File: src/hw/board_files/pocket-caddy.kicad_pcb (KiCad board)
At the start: 4 copper layers, 68 x 100 mm, 90 parts, among them J1 USB_C_Receptacle_USB2.0_14P, J2 Screw_Terminal_01x03, J3 Conn_01x03_Pin, J4 Test_Points, J5 Conn_01x04, J6 Molex 104031-0811, Q1 PMOS, SW1 SW_PWR, SW2 RESET, SW3 BTN_2, SW4 BTN_3, SW5 BTN_1_BOOT, U1 MCP73871, U2 TPS63031DSKR, U3 ESP32-C3-WROOM-02, U4 NEO-M9N, U5 SHT30-DIS, U6 BQ27411DRZT-G1A, Y1 32.768kHz

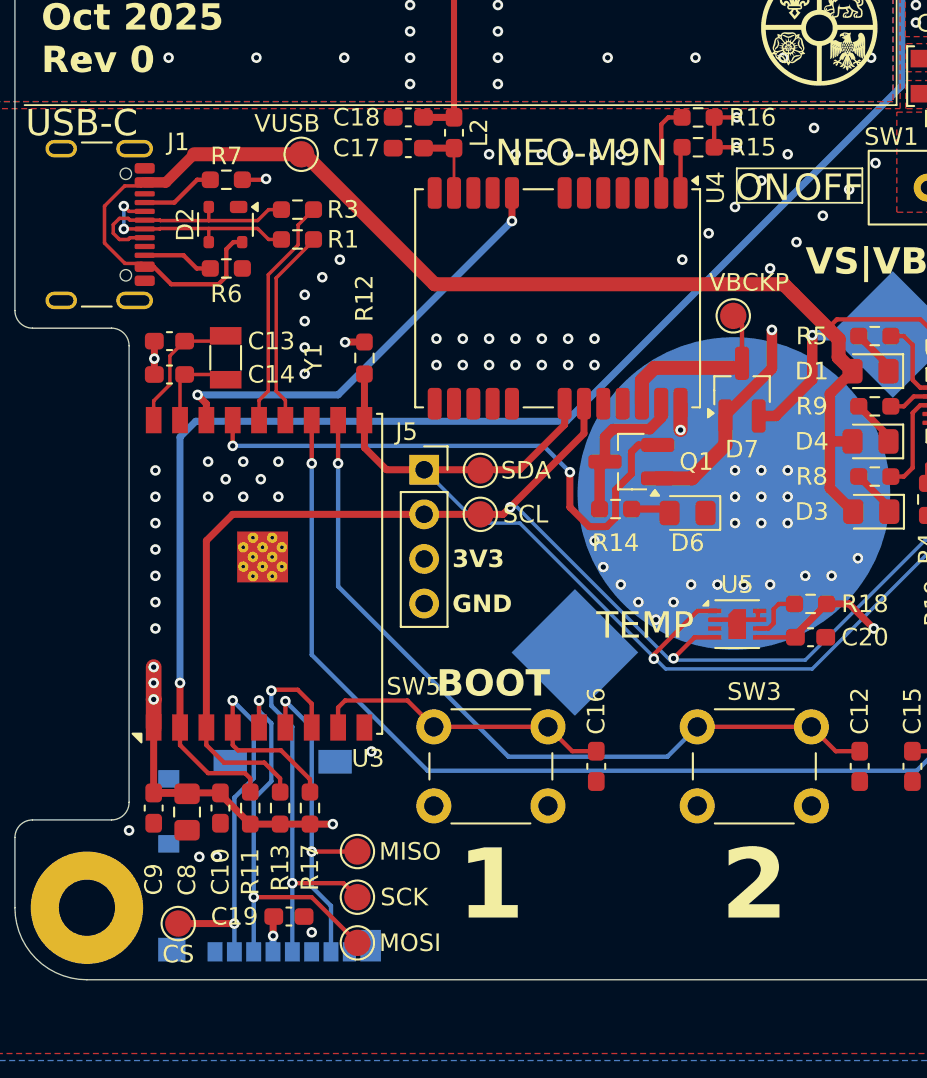
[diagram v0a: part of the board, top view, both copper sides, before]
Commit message: Initial commit, fixed esp enable RC delay circuit
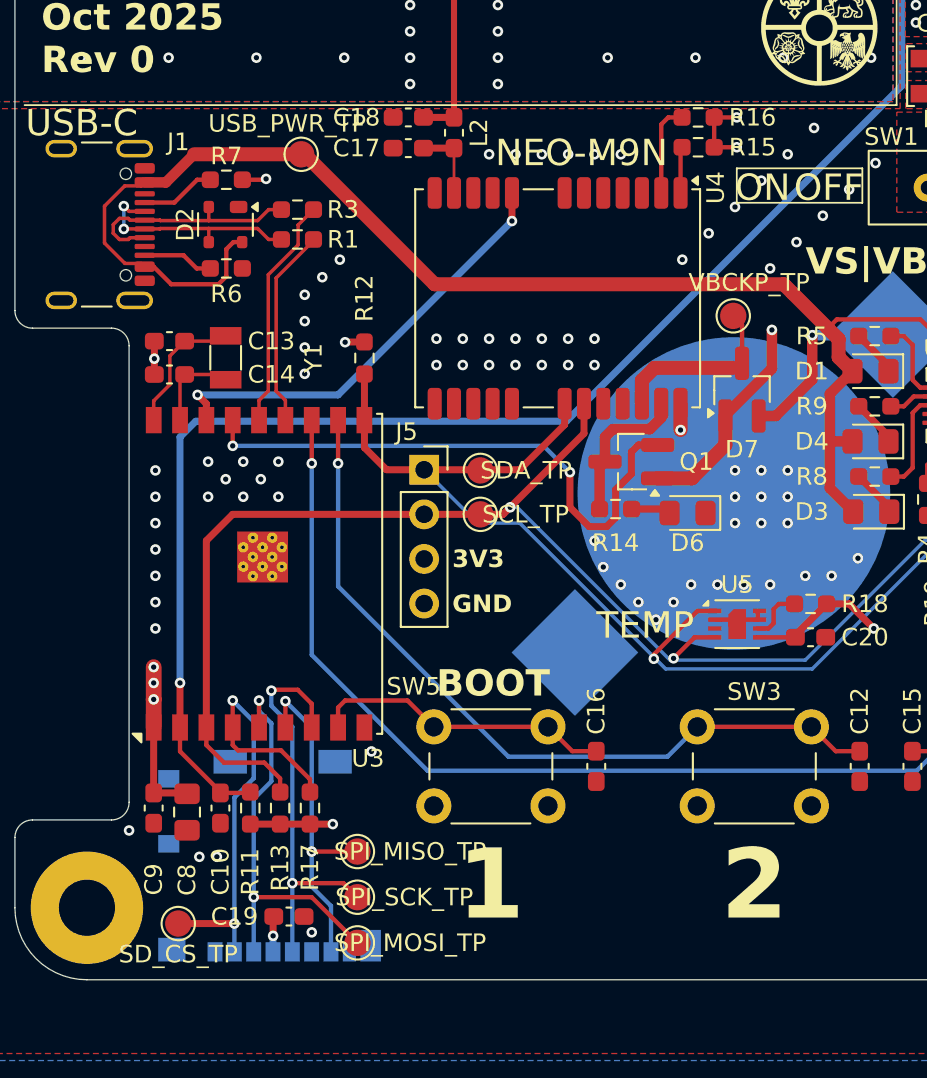
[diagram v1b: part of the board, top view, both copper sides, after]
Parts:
- TP1: value SCL -> SCL_TP
- TP2: value SDA -> SDA_TP
- TP3: value CS -> SD_CS_TP
- TP4: value MOSI -> SPI_MOSI_TP
- TP5: value MISO -> SPI_MISO_TP
- TP6: value SCK -> SPI_SCK_TP
- TP7: value VUSB -> USB_PWR_TP
- TP8: value VBCKP -> VBCKP_TP
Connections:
- C10 pad 2: +3V3 -> Net-(U3-EN)
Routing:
- net +3V3: track 57.5 -> 51.2 mm

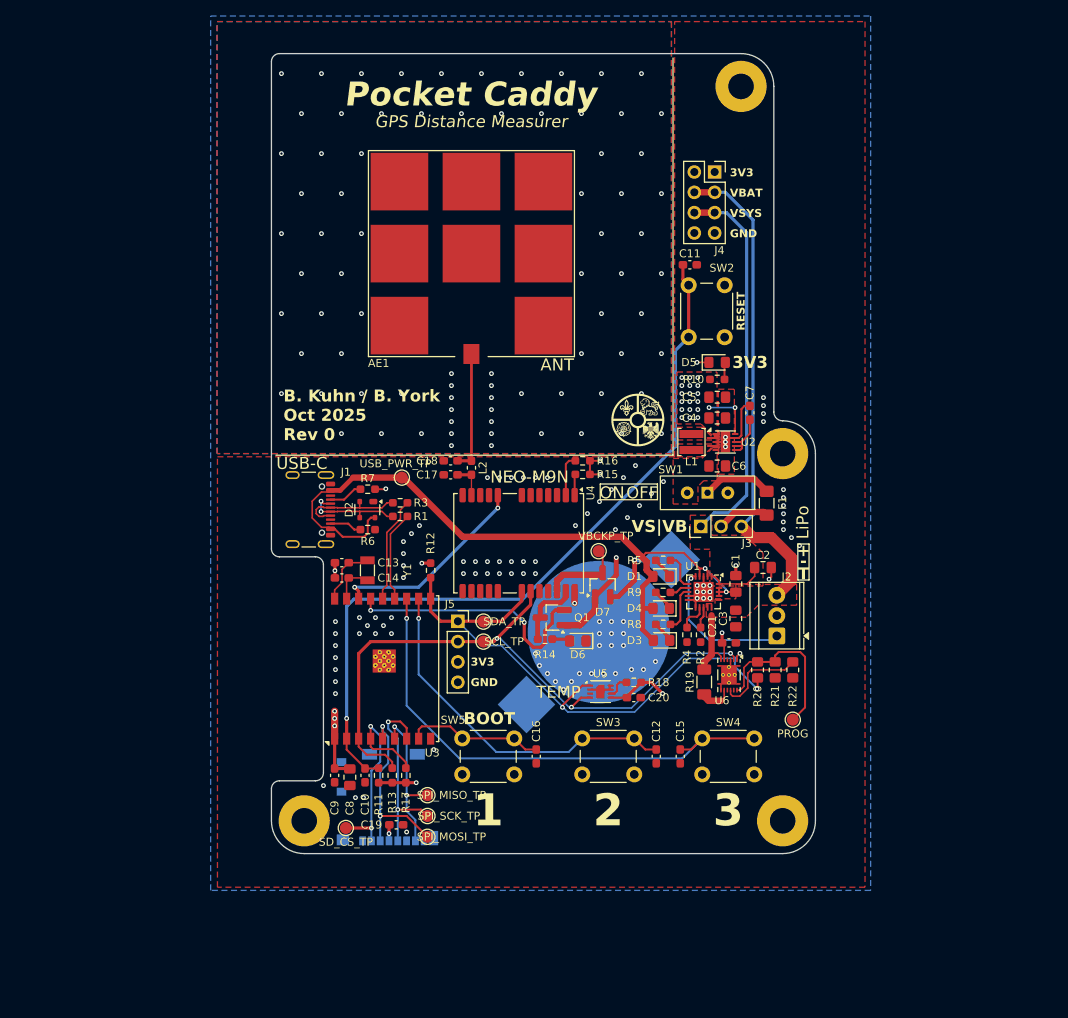
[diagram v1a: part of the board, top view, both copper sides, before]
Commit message: Added new OLED footprint. Finished schematic updates, started lyout. Changed 10 mOhm sense resistor PN to TCR of 50 ppm/C
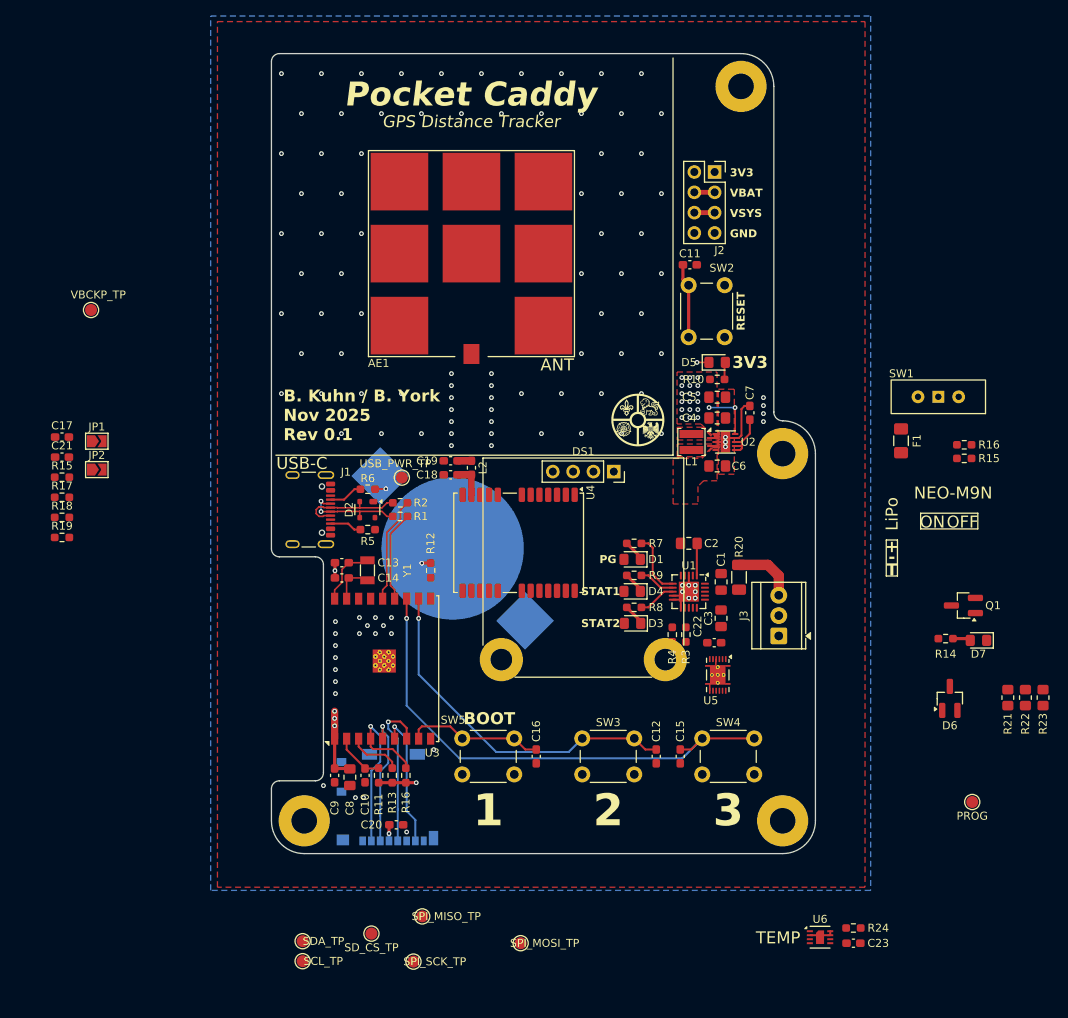
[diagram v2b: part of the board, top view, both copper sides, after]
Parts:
- removed the J2 at (223.2, 102.8)
- removed J5: Conn_01x04, Connector_PinSocket_2.54mm:PinSocket_1x04_P2.54mm_Vertical
- added C17: 100n, Capacitor_SMD:C_0603_1608Metric_Pad1.08x0.95mm_HandSolder, F.Cu at (133.8, 77.9)
- added C21: 1u, Capacitor_SMD:C_0603_1608Metric_Pad1.08x0.95mm_HandSolder, F.Cu at (133.8, 80.4)
- added DS1: ~, Project_Library:OLED_128x64_0.96in, F.Cu at (202.8, 82.2)
- added JP1: Solder_Jumper, Jumper:SolderJumper-2_P1.3mm_Open_TrianglePad1.0x1.5mm, F.Cu at (138.2, 78.5)
- added JP2: Solder_Jumper, Jumper:SolderJumper-2_P1.3mm_Open_TrianglePad1.0x1.5mm, F.Cu at (138.2, 82.0)
- added R15: 10k, Resistor_SMD:R_0603_1608Metric_Pad0.98x0.95mm_HandSolder, F.Cu at (133.8, 83.0)
- added R17: 10k, Resistor_SMD:R_0603_1608Metric_Pad0.98x0.95mm_HandSolder, F.Cu at (133.8, 85.5)
- added R18: 10k, Resistor_SMD:R_0603_1608Metric_Pad0.98x0.95mm_HandSolder, F.Cu at (133.8, 88.0)
- added R19: 10k, Resistor_SMD:R_0603_1608Metric_Pad0.98x0.95mm_HandSolder, F.Cu at (133.8, 90.5)
- J3: value Conn_01x03_Pin -> Screw_Terminal_01x03; footprint Connector_PinHeader_2.54mm:PinHeader_1x03_P2.54mm_Vertical -> TerminalBlock_TE-Connectivity:TerminalBlock_TE_282834-3_1x03_P2.54mm_Horizontal
- R12, R13: value 10k -> 4k7
- moved TP8 70.2 mm to (137.4, 62.0)
- moved Q1 51.4 mm to (246.5, 99.0)
- moved R14 50.1 mm to (244.3, 103.1)
- moved D7 50.1 mm to (248.4, 103.3)
- moved R15 47.7 mm to (246.6, 80.6)
- moved R16 47.7 mm to (246.6, 78.9)
- moved TP1 45.9 mm to (163.9, 143.4)
- moved TP2 45.9 mm to (163.9, 140.9)
- moved D6 45.7 mm to (244.8, 110.6)
- moved R24 41.2 mm to (232.8, 139.3)
- moved C23 41.2 mm to (232.8, 141.2)
- moved U6 41.2 mm to (228.6, 140.4)
- moved R21 31.5 mm to (252.1, 110.5)
- moved R22 31.5 mm to (254.2, 110.5)
- moved R23 31.5 mm to (256.4, 110.5)
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- renumbered BT2 to BT1, C17 to C18, C18 to C19, C19 to C20, C21 to C22, C20 to C23, D7 to D6, D6 to D7, J4 to J2, J6 to J4, R17 to R16, R3 to R2, R19 to R20, R20 to R21, R21 to R22, R22 to R23, R18 to R24, R2 to R3, R6 to R5, R7 to R6, R5 to R7, U6 to U5, U5 to U6
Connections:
- C22 pad 2: +3V3 -> Net-(U5-V_{DD})
- F1 pad 1: Net-(J3-Pin_2) -> V_SYS
- J3 pad 1: V_SYS -> /Peripherals/NTC_THERM
- J3 pad 2: Net-(J3-Pin_2) -> GND
- J3 pad 3: VBAT -> /Peripherals/VBAT_IN
- Q1 pad 1: +3V3 -> Net-(Q1-D)
- Q1 pad 3: Net-(Q1-S) -> +3V3
- R14 pad 1: Net-(Q1-S) -> Net-(Q1-D)
- R20 pad 1: VBAT -> /Peripherals/VBAT_IN
- R20 pad 2: Net-(U6-SRP) -> VBAT
- U1 pad 5: /USB-C and Power/NTC_THERM -> /Peripherals/NTC_THERM
- U4 pad 1: Net-(U4-~{SAFEBOOT}) -> Net-(JP1-B)
- U4 pad 2: Net-(U4-D_SEL) -> Net-(JP2-B)
- U4 pad 23: Net-(Q1-S) -> Net-(Q1-D)
- U5 pad 5: +3V3 -> Net-(U5-V_{DD})
- U5 pad 6: VBAT -> /Peripherals/VBAT_IN
- U5 pad 7: GND -> VBAT
- U5 pad 8: Net-(U6-SRP) -> /Peripherals/VBAT_IN
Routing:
- net V_USB: track 92.9 -> 0.00 mm, vias 2 -> 0
- net Net-(U3-EN): track 96.2 -> 15.8 mm, vias 1 -> 0
- net /SCL: track 82.7 -> 6.76 mm, vias 3 -> 0
- net /SDA: track 73.5 -> 0.00 mm, vias 3 -> 0
- net VBAT: track 70.0 -> 2.54 mm
- net V_SYS: track 55.2 -> 6.58 mm
- net /Microcontroller/GPS_~{EN}: track 32.3 -> 0.00 mm, vias 2 -> 0
- net +3V3: track 51.2 -> 23.5 mm, vias 31 -> 26
- net /Microcontroller/GPS_~{RESET}: track 25.2 -> 0.00 mm, vias 2 -> 0
- net Net-(U5-PROG): track 21.5 -> 0.00 mm
- net /USB-C and Power/NTC_THERM: track 18.2 -> 0.00 mm, vias 1 -> 0
- net Net-(U5-TEST): track 11.2 -> 0.00 mm
- net Net-(BT1-+): track 11.0 -> 0.00 mm, vias 1 -> 2
- net V_BCKP: track 9.73 -> 0.00 mm
- net Net-(SW1-B): track 8.72 -> 0.00 mm
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- removed copper zone on F.Cu, net VBAT
- removed copper zone on F.Cu, net V_SYS
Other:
- board text added: "B. Kuhn / B. York Nov 2025 Rev 0.1"
- board text added: "GPS Distance Tracker"
- board text added: "PG"
- board text added: "STAT1"
- board text added: "STAT2"
- board text removed: "B. Kuhn / B. York Oct 2025 Rev 0"
- board text removed: "GPS Distance Measurer"
- board text removed: "VS|VB"

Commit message: Layout progress
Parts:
- removed JP1, JP2: Solder_Jumper, Jumper:SolderJumper-2_P1.3mm_Open_TrianglePad1.0x1.5mm
- removed the R15 at (246.6, 80.6)
- removed the R16 at (246.6, 78.9)
- TP1: value SCL_TP -> SCL; footprint TestPoint:TestPoint_Pad_D1.5mm -> TestPoint:TestPoint_Pad_D1.0mm
- TP2: value SDA_TP -> SDA; footprint TestPoint:TestPoint_Pad_D1.5mm -> TestPoint:TestPoint_Pad_D1.0mm
- TP3, TP4, TP5, TP6, TP7, TP8, TP9: footprint TestPoint:TestPoint_Pad_D1.5mm -> TestPoint:TestPoint_Pad_D1.0mm
- moved TP8 114.1 mm to (239.2, 113.5)
- moved C21 88.8 mm to (218.6, 106.8), turned to 90 degrees
- moved TP7 74.5 mm to (244.3, 113.5), turned to 0 degrees
- moved C17 66.9 mm to (196.8, 100.6), turned to 90 degrees
- moved R18 57.9 mm to (181.9, 120.2), turned to 90 degrees
- moved R17 56.6 mm to (178.5, 120.2), turned to 90 degrees
- moved D7 55.3 mm to (193.1, 100.8), turned to -90 degrees
- moved R19 55.1 mm to (180.2, 120.2), turned to 90 degrees
- moved R14 49.2 mm to (195.1, 100.6), turned to -90 degrees
- moved Q1 47.5 mm to (199.4, 105.1), turned to -90 degrees
- moved R15 45.9 mm to (178.2, 94.6), turned to 90 degrees
- moved TP2 44.8 mm to (182.5, 100.2), turned to 180 degrees
- moved TP1 44.6 mm to (182.4, 102.9)
- moved R24 42.5 mm to (202.9, 109.0)
- moved C23 42.5 mm to (202.9, 110.9)
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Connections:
- U4 pad 1: Net-(JP1-B) -> +3V3
- U4 pad 2: Net-(JP2-B) -> +3V3
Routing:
- net V_USB: track 0.00 -> 104.0 mm, vias 0 -> 3
- net /SDA: track 0.00 -> 77.3 mm, vias 0 -> 2
- net /SCL: track 6.76 -> 82.8 mm
- net /Microcontroller/BTN_3: track 63.9 -> 9.82 mm, vias 1 -> 0
- net /Microcontroller/BTN_2: track 44.5 -> 9.82 mm, vias 1 -> 0
- net Net-(U5-TEST): track 0.00 -> 25.9 mm
- net /Peripherals/VBAT_IN: track 7.97 -> 32.9 mm
- net +3V3: track 23.5 -> 46.2 mm, vias 26 -> 30
- net Net-(U5-PROG): track 0.00 -> 20.6 mm
- net GND: track 21.7 -> 41.5 mm, vias 115 -> 154
- net Net-(BT1-+): track 0.00 -> 15.4 mm, vias 2 -> 1
- net V_BCKP: track 0.00 -> 14.6 mm
- net Net-(Q1-D): track 0.00 -> 10.4 mm
- net VBAT: track 2.54 -> 11.7 mm
- net Net-(SW1-B): track 0.00 -> 6.47 mm
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- added copper zone on F.Cu, net VBAT
- added copper zone on F.Cu, net V_SYS
- added copper zone on F.Cu, net V_USB
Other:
- board text added: "GPS"
- board text added: "ST1"
- board text removed: "STAT1"
- board text removed: "STAT2"

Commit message: Layout progress
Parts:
- removed TP3: SD_CS_TP, TestPoint:TestPoint_Pad_D1.0mm
- removed TP4: SPI_MOSI_TP, TestPoint:TestPoint_Pad_D1.0mm
- removed TP5: SPI_MISO_TP, TestPoint:TestPoint_Pad_D1.0mm
- removed TP6: SPI_SCK_TP, TestPoint:TestPoint_Pad_D1.0mm
- TP7: value USB_PWR_TP -> VUSB
- moved TP7 74.4 mm to (176.3, 83.3), turned to 180 degrees
- moved VBCKP 44.9 mm to (200.2, 91.4)
- moved G*** 35.3 mm to (216.3, 42.1)
- moved R20 6.04 mm to (218.7, 101.5), turned to 90 degrees
- moved C3 5.00 mm to (218.7, 96.2), turned to 90 degrees
- moved J2 3.82 mm to (215.4, 48.6)
- moved C11 3.60 mm to (212.3, 60.0)
- moved SW2 3.60 mm to (216.7, 62.5)
- turned R15 to -90 degrees
- renumbered TP8 to VBCKP
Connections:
- U3 pad 12: /Microcontroller/BTN_3 -> /Microcontroller/GPS_~{RESET}
- U3 pad 16: /Microcontroller/GPS_~{RESET} -> /Microcontroller/BTN_3
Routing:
- net Net-(U3-EN): track 15.7 -> 120.2 mm, vias 0 -> 3
- net /Microcontroller/BTN_3: track 9.82 -> 65.4 mm, vias 0 -> 1
- net /Microcontroller/GPS_~{RESET}: track 0.00 -> 41.7 mm, vias 0 -> 2
- net /Microcontroller/GPS_~{EN}: track 0.00 -> 34.9 mm, vias 0 -> 2
- net /Microcontroller/BTN_2: track 9.82 -> 40.8 mm, vias 0 -> 2
- net /SCL: track 82.8 -> 104.3 mm, vias 0 -> 2
- net /Peripherals/NTC_THERM: track 0.00 -> 19.9 mm, vias 0 -> 1
- net /SDA: track 77.3 -> 95.1 mm, vias 2 -> 4
- net +3V3: track 46.2 -> 60.4 mm, vias 30 -> 31
- net /Peripherals/VBAT_IN: track 32.9 -> 20.8 mm, vias 0 -> 2
- net V_BCKP: track 14.6 -> 20.7 mm
- net VBAT: track 11.7 -> 7.42 mm
- net GND: track 41.5 -> 43.3 mm, vias 154 -> 155
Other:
- board text removed: "Pocket Caddy Rev. A B. Kuhn, B. York Oct 2025"

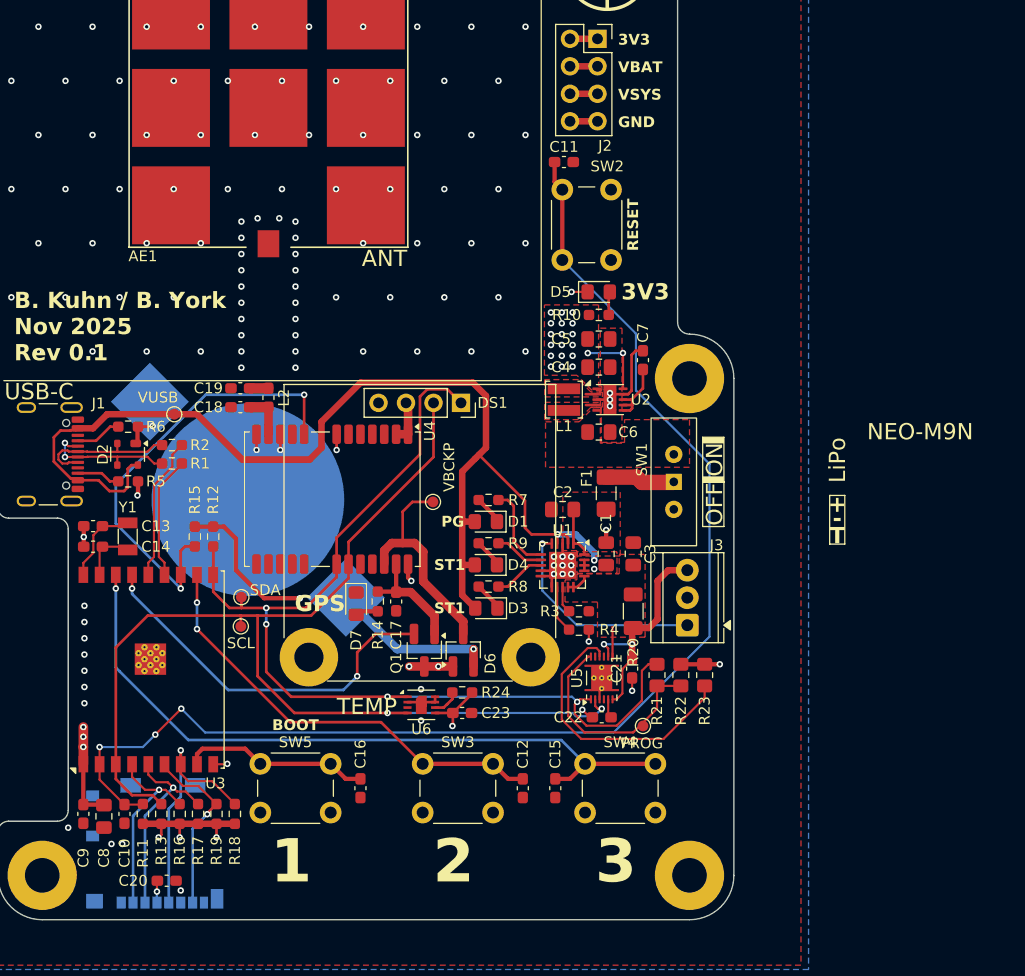
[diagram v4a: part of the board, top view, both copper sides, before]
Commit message: New layout done, need to make gerbers
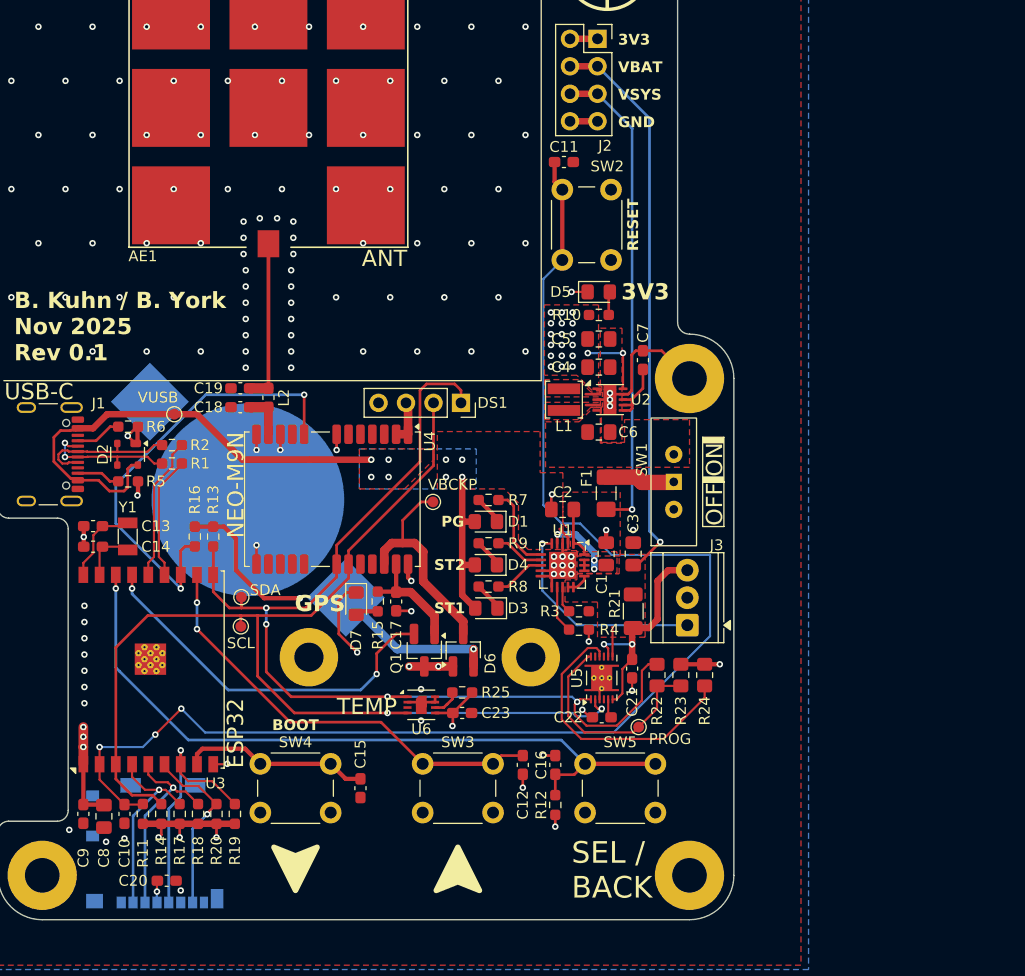
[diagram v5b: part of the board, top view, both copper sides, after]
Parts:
- added R12: 10k, Resistor_SMD:R_0603_1608Metric_Pad0.98x0.95mm_HandSolder, F.Cu at (211.5, 119.4)
- moved C12 2.15 mm to (208.5, 115.7)
- moved C16 2.15 mm to (211.5, 115.7), turned to -90 degrees
- moved TP5 0.41 mm to (219.2, 112.2)
- renumbered C16 to C15, C15 to C16, R12 to R13, R13 to R14, R14 to R15, R15 to R16, R16 to R17, R17 to R18, R18 to R19, R19 to R20, R20 to R21, R21 to R22, R22 to R23, R23 to R24, R24 to R25, SW5 to SW4, SW4 to SW5, TP7 to TP3, TP9 to TP5
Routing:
- net VBAT: track 7.42 -> 57.2 mm, vias 0 -> 1
- net V_SYS: track 7.41 -> 49.5 mm, vias 0 -> 1
- net V_USB: track 104.0 -> 69.2 mm, vias 3 -> 11
- net GND: track 43.3 -> 64.0 mm, vias 155 -> 162
- net Net-(U3-EN): track 120.2 -> 128.0 mm
- net /Microcontroller/BTN_3: track 65.4 -> 67.2 mm
- net /SDA: track 95.1 -> 96.5 mm
- net +3V3: track 60.4 -> 61.4 mm, vias 31 -> 32
- added copper zone on B.Cu, net V_USB
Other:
- board text added: "ESP32"
- board text added: "SEL / BACK"
- board text added: "ST2"
- board text added: "THERM"
- board text removed: "+"
- board text removed: "-"
- board text removed: "1"
- board text removed: "2"
- board text removed: "3"
- board text removed: "LiPo"
- board text removed: "T"
